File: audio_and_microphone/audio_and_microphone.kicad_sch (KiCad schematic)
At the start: 36 parts, among them J2 Conn_01x02, U1 LM4810, U2 ${SIM.PARAMS}, U3 ${SIM.PARAMS}

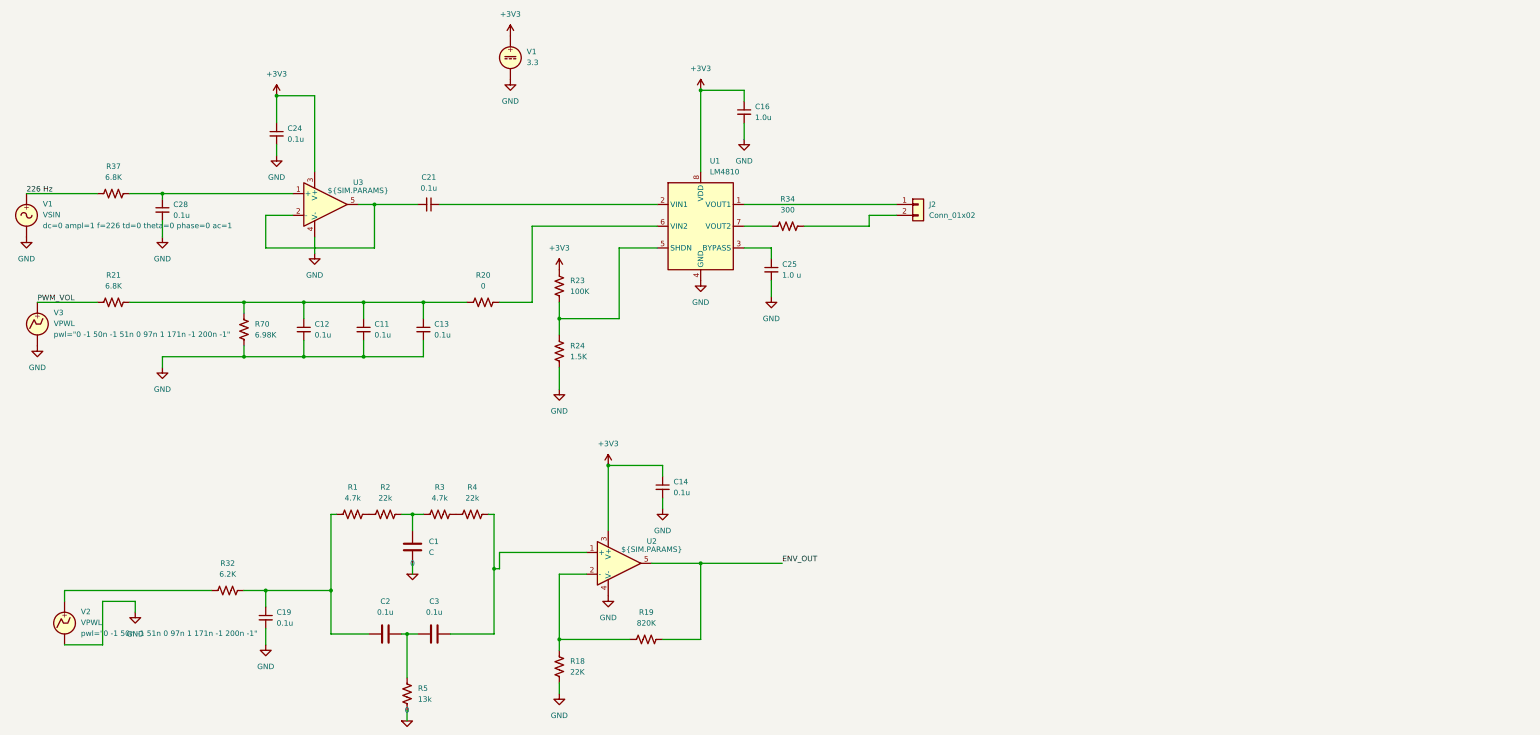
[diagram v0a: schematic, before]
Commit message: Merge firmware from james-oled and PCB from pcb into main
Co-Authored-By: Claude Sonnet 4.6 <noreply@anthropic.com>
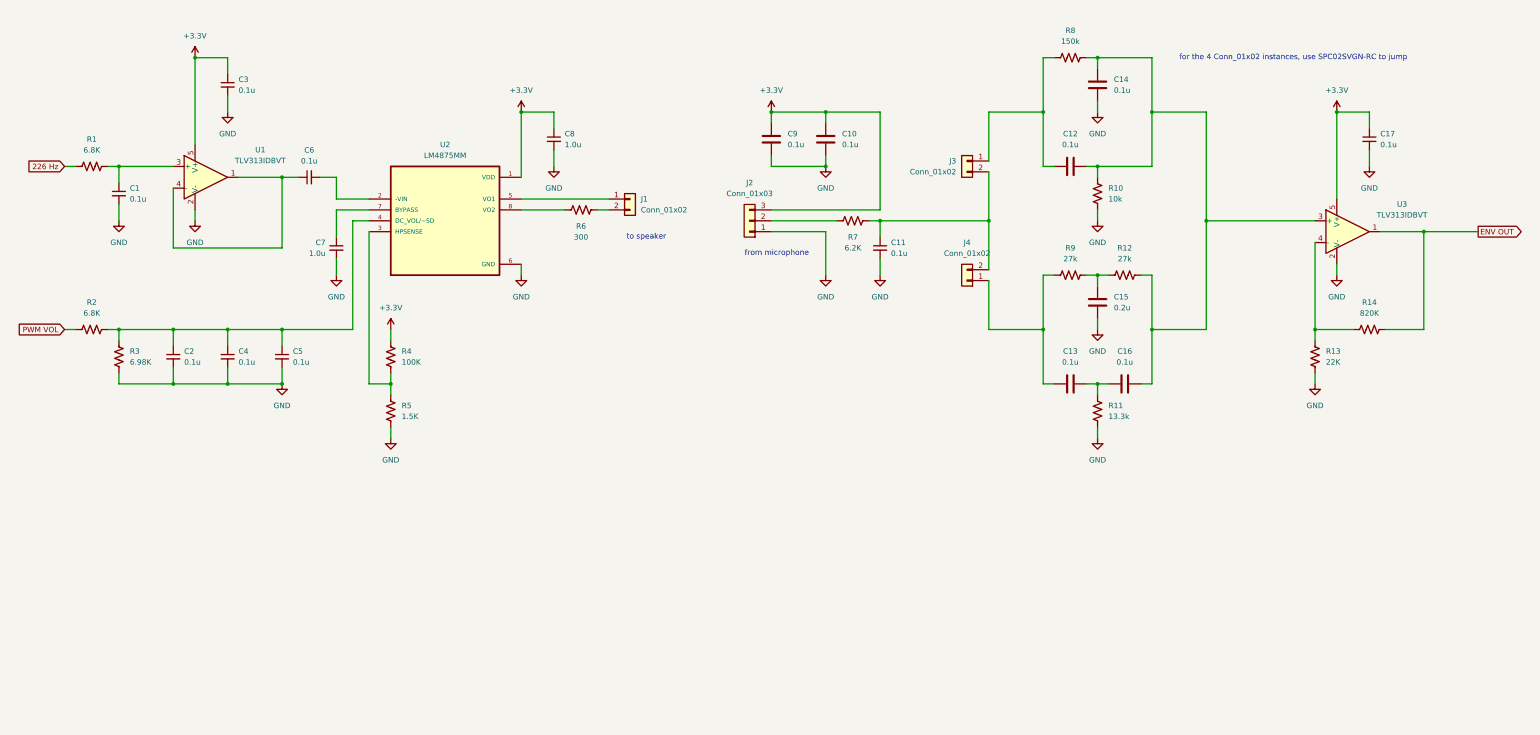
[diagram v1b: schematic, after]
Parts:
- removed R2, R4: 22k, symbol Device:R_US
- removed R20: 0, symbol Device:R_US
- removed U1: LM4810, Package_SO:TSSOP-8_3x3mm_P0.65mm, symbol Amplifier_Audio:LM4810
- removed U2, U3: ${SIM.PARAMS}, symbol Simulation_SPICE:OPAMP
- removed V1: VSIN, symbol Simulation_SPICE:VSIN
- removed V1: 3.3, symbol Simulation_SPICE:VDC
- removed V2, V3: VPWL, symbol Simulation_SPICE:VPWL
- added C10, C12, C14, C9: 0.1u, footprints:CAPC17595_95N_KEM-M, symbol Device:C
- added J2: Conn_01x03, Connector_PinHeader_2.54mm:PinHeader_1x03_P2.54mm_Vertical, symbol Connector_Generic:Conn_01x03
- added J3, J4: Conn_01x02, Connector_PinHeader_2.54mm:PinHeader_1x02_P2.54mm_Vertical, symbol Connector_Generic:Conn_01x02
- added R10: 10k, footprints:RC0603N_YAG-M, symbol Device:R_US
- added R8: 150k, footprints:RC0603N_YAG-M, symbol Device:R_US
- added U1, U3: TLV313IDBVT, Package_TO_SOT_SMD:TSOT-23-5, symbol Amplifier_Operational:AD8603
- added U2: LM4875MM, footprints:SOP65P490X110-8N, symbol LM4875MM:LM4875MM
- C1: renamed from C28; footprint (none) -> footprints:CAPC17595_95N_KEM-M
- C11: renamed from C19; footprint (none) -> footprints:CAPC17595_95N_KEM-M
- C13: renamed from C2; footprint (none) -> footprints:CAPC17595_95N_KEM-M
- C15: renamed from C1; value C -> 0.2u; footprint (none) -> footprints:CAPC17595_95N_KEM-M
- C16: renamed from C3; footprint (none) -> footprints:CAPC17595_95N_KEM-M
- C17: renamed from C14; footprint (none) -> footprints:CAPC17595_95N_KEM-M
- C2: renamed from C12; footprint (none) -> footprints:CAPC17595_95N_KEM-M
- C3: renamed from C24; footprint (none) -> footprints:CAPC17595_95N_KEM-M
- C4: renamed from C11; footprint (none) -> footprints:CAPC17595_95N_KEM-M
- C5: renamed from C13; footprint (none) -> footprints:CAPC17595_95N_KEM-M
- C6: renamed from C21; footprint (none) -> footprints:CAPC17595_95N_KEM-M
- C7: renamed from C25; value 1.0 u -> 1.0u; footprint (none) -> footprints:CAPC17595_95N_KEM-M
- C8: renamed from C16; footprint (none) -> footprints:CAPC17595_95N_KEM-M
- J1: renamed from J2; footprint (none) -> Connector_PinHeader_2.54mm:PinHeader_1x02_P2.54mm_Vertical
- R1: renamed from R37; footprint (none) -> footprints:RC0603N_YAG-M
- R11: renamed from R5; value 13k -> 13.3k; footprint (none) -> footprints:RC0603N_YAG-M
- R12: renamed from R3; value 4.7k -> 27k; footprint (none) -> footprints:RC0603N_YAG-M
- R13: renamed from R18; footprint (none) -> footprints:RC0603N_YAG-M
- R14: renamed from R19; footprint (none) -> footprints:RC0603N_YAG-M
- R2: renamed from R21; footprint (none) -> footprints:RC0603N_YAG-M
- R3: renamed from R70; footprint (none) -> footprints:RC0603N_YAG-M
- R4: renamed from R23; footprint (none) -> footprints:RC0603N_YAG-M
- R5: renamed from R24; footprint (none) -> footprints:RC0603N_YAG-M
- R6: renamed from R34; footprint (none) -> footprints:RC0603N_YAG-M
- R7: renamed from R32; footprint (none) -> footprints:RC0603N_YAG-M
- R9: renamed from R1; value 4.7k -> 27k; footprint (none) -> footprints:RC0603N_YAG-M
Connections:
- net 0 is gone; now on net GND: C15.2, R11.2
- net GND: now also C10.1, C14.2, C9.1, J2.1 (Pin_1), R10.2, U1.2 (V-), U2.6 (GND), U3.2 (V-)
- net at C13.1, R9.1: now also J4.1 (Pin_1); no longer C11.1, R7.1
- net at C13.2, R11.1: now also C16.2; no longer C16.1
- net at R4.2, R5.1: now also U2.3 (HPSENSE)
- net at C1.1, R1.1: now also U1.3 (+)
- net at C6.2: now also U2.2 (-VIN)
- net at J1.1 (Pin_1): now also U2.5 (VO1)
- net at R6.2: now also U2.8 (VO2)
- net at C2.1, C4.1, C5.1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: now also U2.4 (DC_VOL/~SD)
- net at R13.1, R14.2: now also U3.4 (-)
- net at R9.2: now also C15.1, R12.1
- net at C6.1: now also U1.1, U1.4 (-)
- net at C7.1: now also U2.7 (BYPASS)
- net at R12.2: now also C16.1, C12.2, C14.1, R10.1, R8.2, U3.3 (+)
- net at R7.2: now also J2.2 (Pin_2)
- net +3V3 renamed +3.3V
- net +3.3V: now also C10.2, C9.2, J2.3 (Pin_3), U1.5 (V+), U2.1 (VDD), U3.5 (V+)
- net ENV_OUT renamed ENV OUT
- net ENV OUT: now also U3.1
- net PWM_VOL renamed PWM VOL
- new net: C12.1, J3.1 (Pin_1), R8.1
- new net: C11.1, J3.2 (Pin_2), J4.2 (Pin_2), R7.1
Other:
- note added: "for the 4 Conn_01x02 instances, use SPC02SVGN-RC to jump"
- note added: "from microphone"
- note added: "to speaker"
- company: (none) -> Alisha Gupta, Iris Ye, James Mu
- title: (none) -> Tympanometer
- moved on the sheet: C1, C11, C13, C15, C16, C17, C2, C3, C4, C5, C6, C7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
